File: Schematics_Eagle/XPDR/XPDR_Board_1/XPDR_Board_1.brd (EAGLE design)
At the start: 172.7 x 36.8 mm, 40 parts

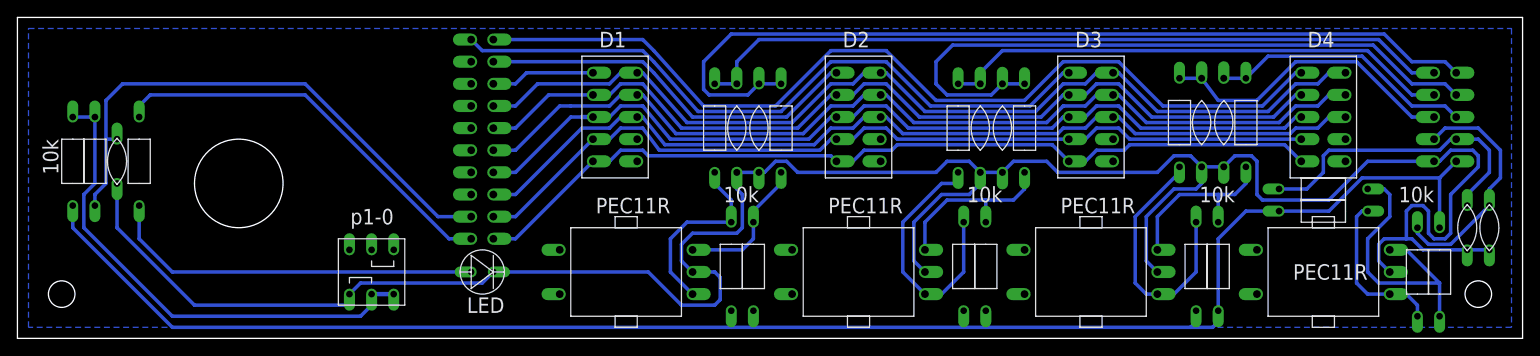
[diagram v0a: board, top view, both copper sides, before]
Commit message: Both XPDR boards finished.
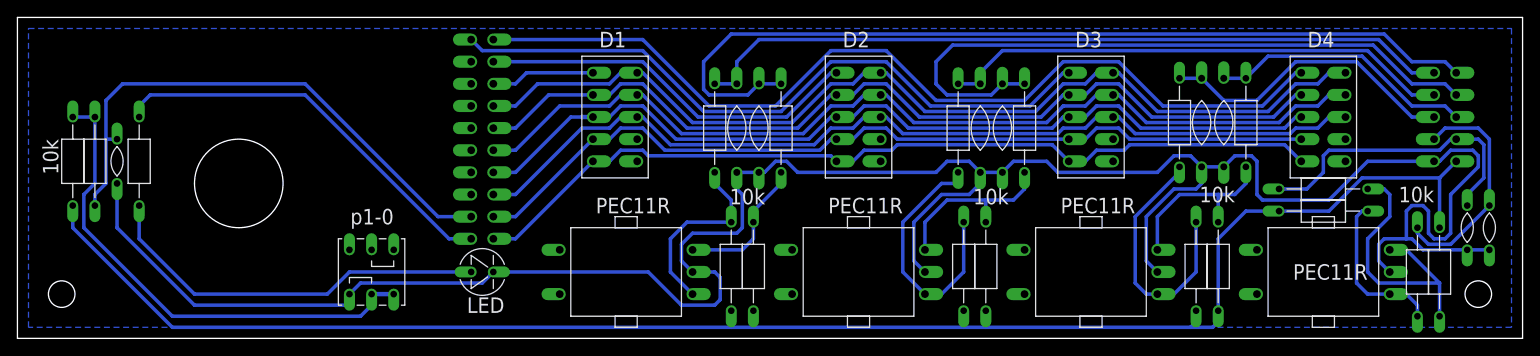
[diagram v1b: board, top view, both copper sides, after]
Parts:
- U$1, U$2, U$3, U$4: device RadioStack_v2:PEC11R -> library:PEC11R
- U$10: device RadioStack_v2:LED_5MM -> library:LED_5MM
- U$11, U$12, U$13, U$14, U$15, U$16, U$19, U$20, U$21, U$22, U$23, U$24, U$25, U$26, U$27, U$28, U$30, U$31, U$40: value (none) -> REZISTOR; device RadioStack_v2:REZISTOR -> library:REZISTOR
- U$17: device RadioStack_v2:LISTA_2X5 -> library:LISTA_2X5
- U$18: device RadioStack_v2:LISTA_2X10 -> library:LISTA_2X10
- U$29, U$32, U$33, U$35, U$36, U$37: device RadioStack_v2:KONDENZATOR_SIROKY -> library:KONDENZATOR_SIROKY
- U$34, U$38, U$39: device RadioStack_v2:KONDENZATOR -> library:KONDENZATOR
- U$5, U$6, U$7, U$8: device RadioStack_v2:SA3611EWA -> library:SA3611EWA
- U$9: device RadioStack_v2:P1-0S -> library:P1-0S
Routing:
- net N$32: track 43.5 -> 45.6 mm
- net N$14: track 27.3 -> 26.3 mm
- net N$30: track 35.5 -> 35.0 mm
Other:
- board text added: "Enc1A"
- board text added: "Enc1B"
- board text added: "Enc2A"
- board text added: "Enc2B"
- board text added: "Enc3A"
- board text added: "Enc3B"
- board text added: "Enc4A"
- board text added: "Enc4B"
- board text removed: "Enc1 A"
- board text removed: "Enc1 B"
- board text removed: "Enc2 A"
- board text removed: "Enc2 B"
- board text removed: "Enc3 A"
- board text removed: "Enc3 B"
- board text removed: "Enc4 A"
- board text removed: "Enc4 B"
